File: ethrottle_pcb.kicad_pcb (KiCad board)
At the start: 2 copper layers, 41 parts, among them J1 ATM15-08PA-BM02, K1 DIP12-1C90-51x, U1 LM4040DBZ-5, U2 LM324, U3 LM324

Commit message: update format
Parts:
- D7: value 1N5401 -> CGRM4007-G; footprint Diode_THT:D_DO-201AD_P15.24mm_Horizontal -> Diode_SMD:D_SOD-123
- moved D9 115.7 mm to (144.8, 48.5), turned to 180 degrees
- moved R20 81.7 mm to (134.6, 48.5), turned to 180 degrees
- moved C2 81.7 mm to (132.1, 46.0), turned to 180 degrees
- moved R15 81.4 mm to (99.1, 46.0)
- moved R5 76.5 mm to (106.7, 48.5)
- moved D7 73.5 mm to (127.0, 48.5), turned to -90 degrees
- moved R4 69.7 mm to (104.1, 47.3)
- moved R21 69.7 mm to (116.8, 46.0)
- moved R23 67.4 mm to (149.9, 63.5), turned to 180 degrees
- moved D11 63.9 mm to (149.9, 65.8), turned to 180 degrees
- moved R22 63.4 mm to (116.8, 48.5), turned to -90 degrees
- moved R16 62.4 mm to (121.9, 48.5)
- moved R17 60.5 mm to (121.9, 51.1)
- moved R19 58.1 mm to (124.5, 53.6), turned to 180 degrees
- moved K1 53.5 mm to (138.4, 58.4)
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
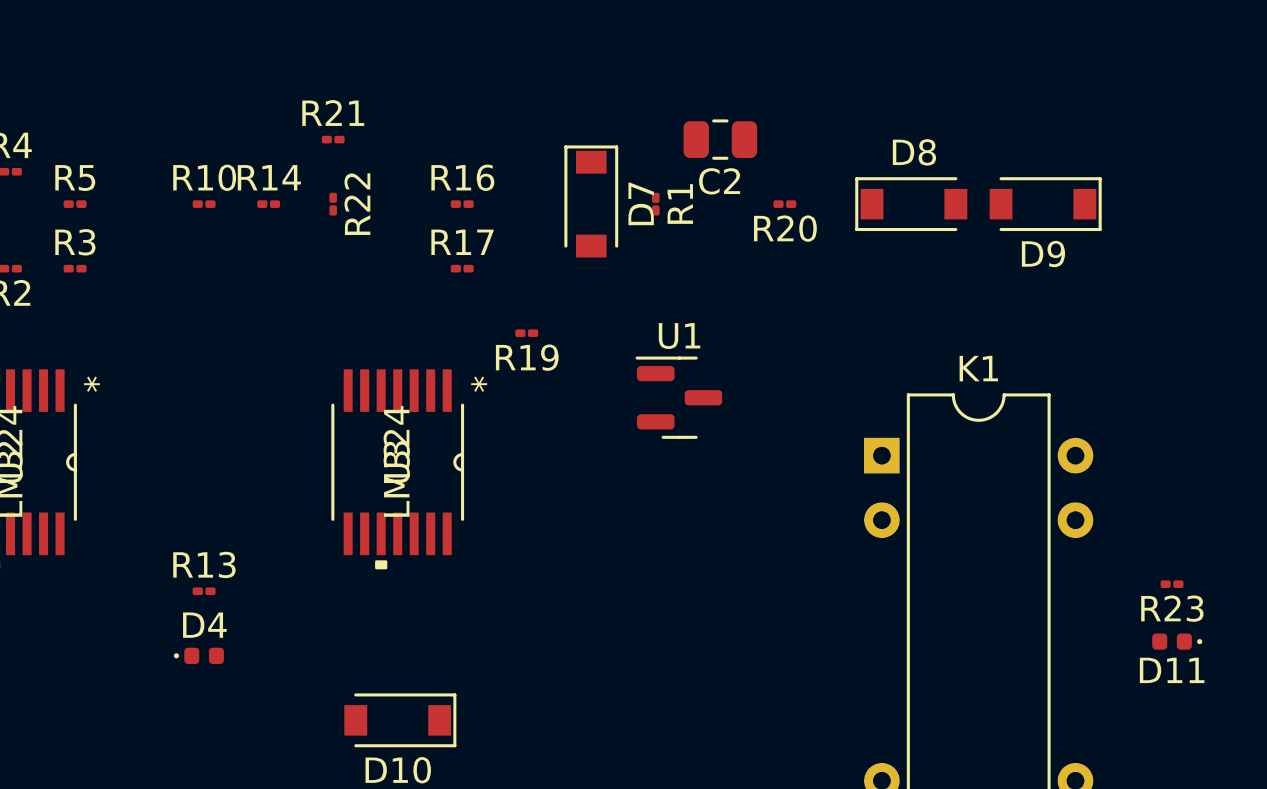
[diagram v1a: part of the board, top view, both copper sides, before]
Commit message: change labels
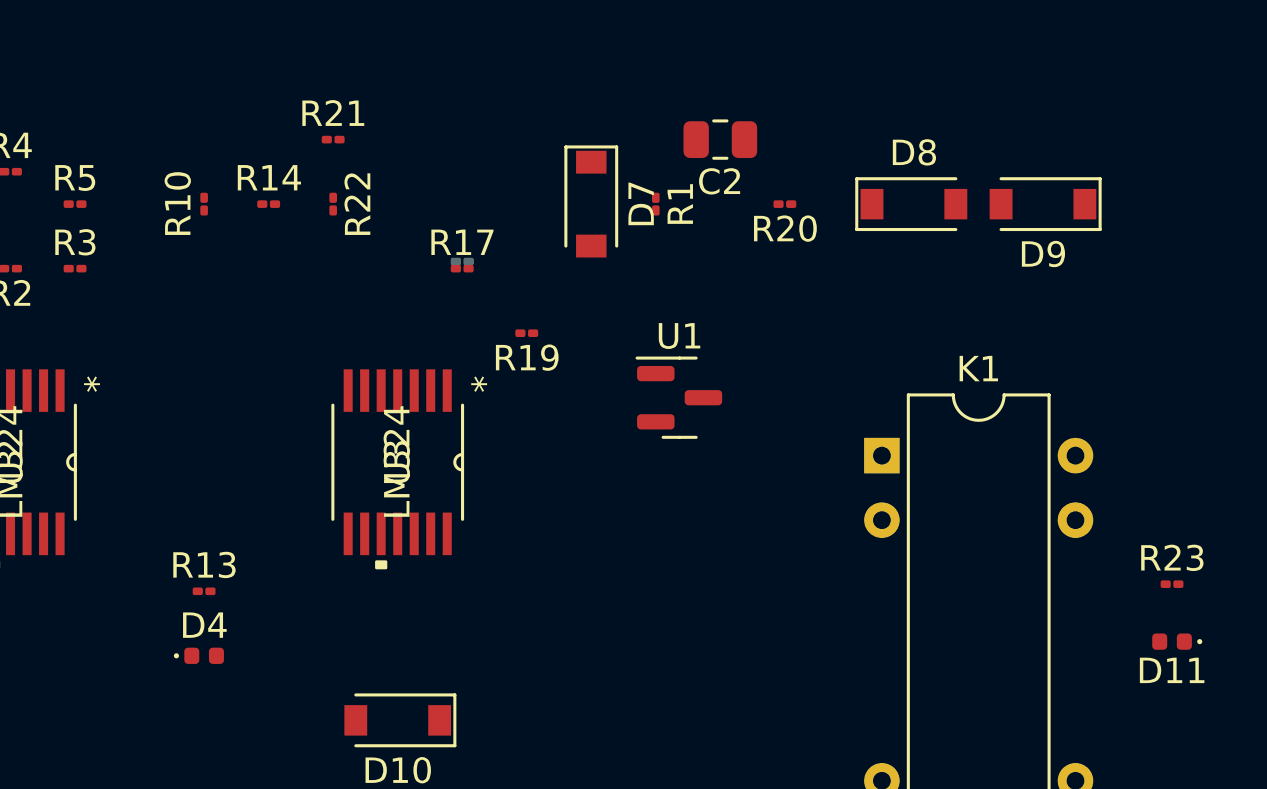
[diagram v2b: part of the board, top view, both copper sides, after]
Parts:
- R16: moved to B.Cu
- moved R16 2.26 mm to (121.9, 50.8), turned to 180 degrees
- turned R10 to 90 degrees
- turned R23 to 0 degrees
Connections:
- net /1V renamed +1V0
- net /2.5V renamed +2V5
- net /4.5V renamed 4.5V
- J1 pad 6: unconnected-(J1-Pad6) -> GND

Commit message: update labels
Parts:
- R7, R9: moved to B.Cu
- moved R7 60.2 mm to (109.2, 45.7), turned to 180 degrees
- moved R6 55.8 mm to (109.3, 45.8)
- moved R9 43.8 mm to (104.0, 65.9), turned to 180 degrees
- moved R8 38.3 mm to (104.1, 68.6)
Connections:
- R1 pad 1: +12V -> +5V
- R1 pad 2: Net-(R1-Pad2) -> +12V
- R16 pad 1: +12V -> +5V
- R2 pad 1: +12V -> +5V
- R21 pad 1: +12V -> +5V
- R3 pad 1: +12V -> +5V
- R4 pad 1: +12V -> +5V
- R6 pad 1: +12V -> +5V
- R8 pad 1: +12V -> +5V
- U1 pad 1: Net-(R1-Pad2) -> +5V

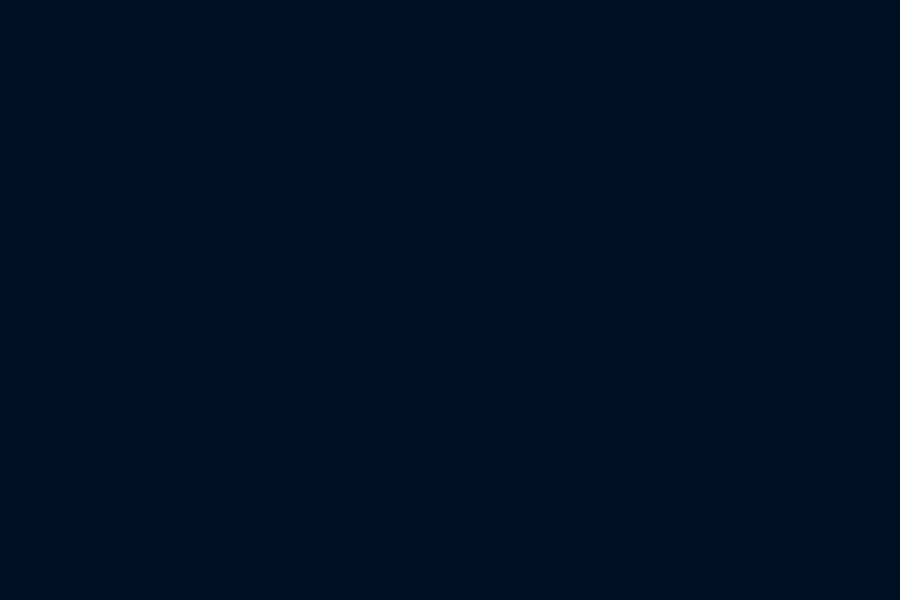
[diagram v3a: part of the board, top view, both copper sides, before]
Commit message: add lm358
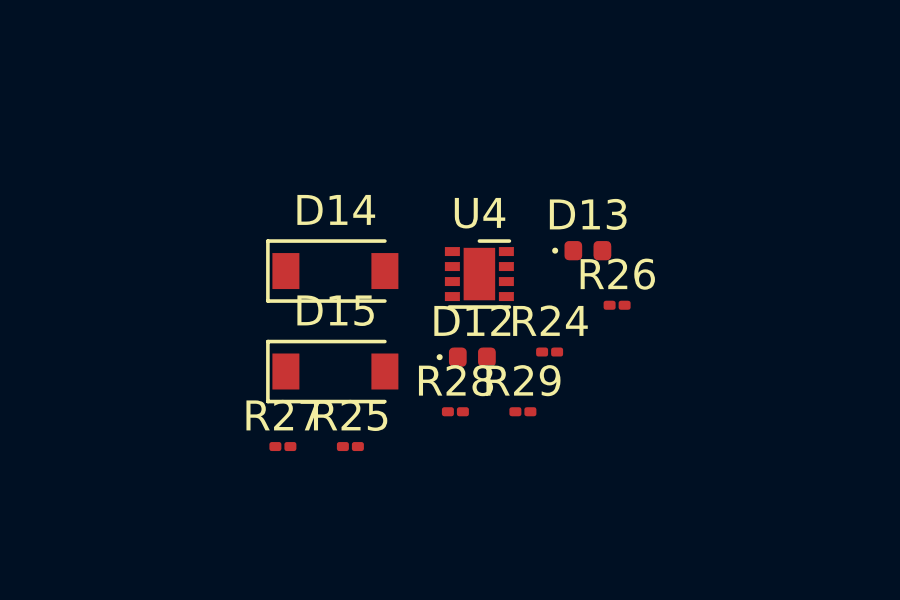
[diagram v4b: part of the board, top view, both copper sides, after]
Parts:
- added D12: LED, LED_SMD:LED_0402_1005Metric, F.Cu at (129.5, 88.9)
- added D13: LED, LED_SMD:LED_0402_1005Metric, F.Cu at (133.4, 85.3)
- added D14: CGRM4007-G, Diode_SMD:D_SOD-123, F.Cu at (125.0, 86.0)
- added D15: CGRM4007-G, Diode_SMD:D_SOD-123, F.Cu at (125.0, 89.4)
- added R24: 100k, Resistor_SMD:R_01005_0402Metric, F.Cu at (132.1, 88.7)
- added R25: 100k, Resistor_SMD:R_01005_0402Metric, F.Cu at (125.5, 91.9)
- added R26: 330, Resistor_SMD:R_01005_0402Metric, F.Cu at (134.4, 87.2)
- added R27: 330, Resistor_SMD:R_01005_0402Metric, F.Cu at (123.2, 91.9)
- added R28: 102k, Resistor_SMD:R_01005_0402Metric, F.Cu at (129.0, 90.7)
- added R29: 11.3k, Resistor_SMD:R_01005_0402Metric, F.Cu at (131.2, 90.7)
- added U4: LM358_DFN, Package_DFN_QFN:DFN-8-1EP_2x2mm_P0.5mm_EP1.05x1.75mm, F.Cu at (129.8, 86.1)

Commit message: adjust layout
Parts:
- removed R6, R7: 10k, Resistor_SMD:R_01005_0402Metric
- R24: moved to B.Cu
- R4: value 10k -> TC33X-2-103E; footprint Resistor_SMD:R_01005_0402Metric -> TC33X-2-103E:TRIM_TC33X-2-103E
- R5: value 2.5k -> TC33X-2-103E; footprint Resistor_SMD:R_01005_0402Metric -> TC33X-2-103E:TRIM_TC33X-2-103E
- moved R29 21.6 mm to (111.8, 81.3), turned to 180 degrees
- moved R28 21.0 mm to (111.8, 78.7)
- moved R24 19.3 mm to (114.3, 81.3), turned to 180 degrees
- moved D13 17.6 mm to (116.8, 91.4)
- moved U4 14.0 mm to (116.8, 80.8)
- moved R26 12.5 mm to (121.9, 86.4)
- moved R25 11.8 mm to (116.8, 83.8)
- moved R4 8.40 mm to (111.8, 50.8)
- moved D15 8.35 mm to (127.0, 81.3), turned to -90 degrees
- moved D12 8.03 mm to (121.9, 91.4), turned to 180 degrees
- moved D10 7.34 mm to (119.2, 76.2)
- moved D11 7.34 mm to (149.7, 73.1)
- moved K1 7.34 mm to (138.2, 65.8)
- moved R9 7.34 mm to (103.8, 73.3)
- moved U2 7.34 mm to (103.9, 66.0)
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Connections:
- R4 pad 2: +1V0 -> TREF
- R5 pad 1: +1V0 -> +5V
- R5 pad 2: GND -> BREF
- U2 pad 2: +1V0 -> TREF
- U2 pad 6: +2V5 -> BREF

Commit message: update constraints & layout
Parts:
- J1: moved to B.Cu
- R16, R24, R9: moved to F.Cu
- moved J1 12.1 mm to (73.4, 67.9), turned to -90 degrees
- moved D9 10.3 mm to (134.6, 58.4), turned to 90 degrees
- moved K1 7.94 mm to (130.8, 68.6)
- moved D11 7.42 mm to (142.2, 73.1)
- moved R23 7.42 mm to (142.2, 70.8)
- moved C1 5.68 mm to (103.9, 86.4)
- moved D12 5.68 mm to (119.4, 86.4)
- moved D13 5.68 mm to (114.3, 86.4)
- moved R24 5.68 mm to (111.8, 76.2), turned to 0 degrees
- moved D8 5.50 mm to (134.6, 53.3), turned to -90 degrees
- moved C2 3.45 mm to (129.5, 50.8)
- moved D7 3.45 mm to (124.5, 53.3)
- moved R1 3.45 mm to (127.0, 53.3), turned to 90 degrees
- moved R20 3.45 mm to (132.1, 53.3)
- moved R17 2.61 mm to (119.1, 58.4)
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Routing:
- added copper zone on F.Cu, net GND

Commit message: some tracess
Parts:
- moved R23 15.2 mm to (127.3, 73.7)
- moved D11 15.0 mm to (127.5, 75.9), turned to 90 degrees
- moved D8 3.57 mm to (131.1, 53.1)
- moved D9 3.56 mm to (131.1, 58.4)
- moved R20 3.34 mm to (128.8, 53.8)
- moved R27 2.84 mm to (124.2, 85.9), turned to -90 degrees
- moved R22 2.34 mm to (114.3, 55.9), turned to 180 degrees
- moved D7 2.05 mm to (122.4, 53.1)
- moved R1 2.05 mm to (125.0, 53.1)
- moved C2 2.05 mm to (127.5, 50.5)
- moved D5 1.98 mm to (103.6, 78.7)
- moved D10 1.80 mm to (116.6, 74.4)
- moved C1 1.76 mm to (105.2, 85.1)
- moved R18 1.76 mm to (105.4, 82.5)
- moved R12 1.72 mm to (100.6, 73.7)
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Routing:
- net Net-(D6-Pad2): track 0.00 -> 13.1 mm
- net Net-(D11-Pad1): track 0.00 -> 10.9 mm
- net Net-(D5-Pad2): track 0.00 -> 10.3 mm
- net Net-(D13-Pad2): track 0.00 -> 9.86 mm, vias 0 -> 1
- net Net-(D5-Pad1): track 0.00 -> 6.06 mm
- net Net-(C1-Pad1): track 0.00 -> 5.71 mm
- net Net-(D10-Pad1): track 0.00 -> 5.60 mm
- net Net-(D10-Pad2): track 0.00 -> 5.58 mm
- net Net-(R11-Pad1): track 0.00 -> 5.11 mm
- net Net-(D12-Pad2): track 0.00 -> 4.75 mm
- net Net-(D3-Pad2): track 0.00 -> 4.34 mm
- net +12V: track 0.00 -> 3.75 mm
- net Net-(D14-Pad2): track 0.00 -> 3.53 mm
- net Net-(C2-Pad1): track 0.00 -> 3.33 mm
- net Net-(D8-Pad1): track 0.00 -> 3.26 mm
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
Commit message: fills & routing
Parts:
- K1: value DIP12-1C90-51x -> 1462042-9; footprint Relay_THT:Relay_StandexMeder_DIP_LowProfile -> ul_1462042-9:1462042-9
- moved R21 24.6 mm to (112.3, 54.1)
- moved R22 24.6 mm to (112.3, 56.6)
- moved R16 22.2 mm to (107.7, 53.8), turned to 180 degrees
- moved R9 16.4 mm to (114.6, 53.4), turned to -90 degrees
- moved J1 14.8 mm to (82.3, 79.7), turned to 90 degrees
- moved R1 14.1 mm to (119.4, 66.0)
- moved D11 14.1 mm to (116.8, 66.0)
- moved U1 14.1 mm to (123.2, 51.3), turned to 180 degrees
- moved D1 13.9 mm to (116.1, 55.9), turned to -90 degrees
- moved R18 13.5 mm to (108.2, 58.4)
- moved D2 13.0 mm to (114.6, 55.9), turned to 90 degrees
- moved D12 12.0 mm to (119.1, 52.2)
- moved D13 12.0 mm to (119.1, 57.5)
- moved R24 12.0 mm to (116.8, 53.0)
- moved R27 11.0 mm to (116.9, 70.1)
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- renumbered D15 to D10, D7 to D11, D8 to D12, D9 to D13, D10 to D14, D11 to D15, D12 to D5, D13 to D6, D5 to D7, D6 to D8, D14 to D9, R12 to R10, R13 to R11, R26 to R12, R27 to R13, R8 to R16, R9 to R17, R16 to R18, R17 to R19, R4 to R2, R18 to R20, R28 to R21, R29 to R22, R19 to R23, R20 to R24, R21 to R25, R22 to R26, R23 to R27, R24 to R3, R25 to R4, R2 to R5, R3 to R6, R5 to R7, R10 to R8, R11 to R9, U4 to U3, U3 to U4
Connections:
- D15 pad 1: Net-(D11-Pad1) -> Net-(D15-Pad1)
- J1 pad 2: GND -> Throttle
- J1 pad 3: Throttle -> Brake
- J1 pad 4: Brake -> GND
- J1 pad 5: Output -> unconnected-(J1-Pad5)
- J1 pad 6: GND -> unconnected-(J1-Pad6)
- J1 pad MH1: unconnected-(J1-PadMH1) -> GND
- J1 pad MH2: unconnected-(J1-PadMH2) -> GND
- J1 pad MH3: unconnected-(J1-PadMH3) -> GND
- J1 pad MH4: unconnected-(J1-PadMH4) -> GND
- K1 pad 1: Output -> Net-(K1-Pad1)
- K1 pad 7: Net-(D11-Pad1) -> unconnected-(K1-Pad7)
- K1 pad 8: Net-(D11-Pad1) -> GND
- U4 pad 14: Net-(K1-Pad2) -> Net-(K1-Pad1)
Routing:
- net GND: track 0.00 -> 23.2 mm, vias 0 -> 20
- net Net-(D8-Pad2): track 13.1 -> 0.00 mm
- net Net-(D11-Pad1): track 10.9 -> 0.00 mm
- net Net-(D13-Pad1): track 5.60 -> 0.00 mm
- net Net-(D14-Pad2): track 5.58 -> 0.00 mm
- net Net-(R15-Pad1): track 5.11 -> 0.00 mm
- net Net-(D7-Pad2): track 10.3 -> 5.78 mm
- net +12V: track 3.75 -> 0.04 mm
- net Net-(C2-Pad1): track 3.33 -> 0.10 mm
- net Net-(D2-Pad2): track 1.81 -> 0.00 mm
- added copper zone on F.Cu, net +12V
- added copper zone on F.Cu, net +5V
- added copper zone on B.Cu, net GND
- removed copper zone on F.Cu, net GND
